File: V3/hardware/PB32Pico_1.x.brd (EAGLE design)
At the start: 33.3 x 10.8 mm, 27 parts, among them IC1 ESP32-PICO-D4UM-ESP32-PICO-D4, U1 AP2112K-3.3TRG1

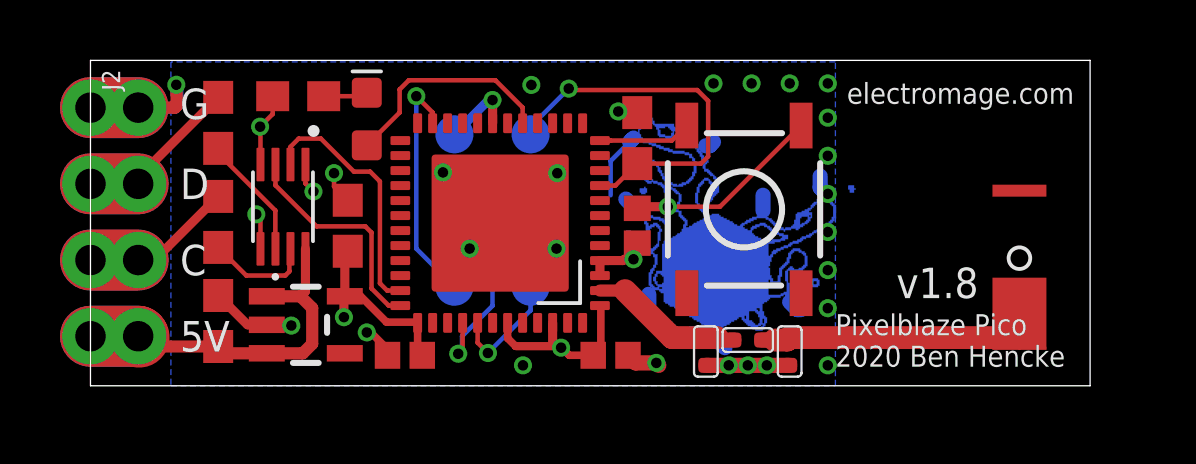
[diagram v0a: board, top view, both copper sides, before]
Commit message: PICO pcb reworked
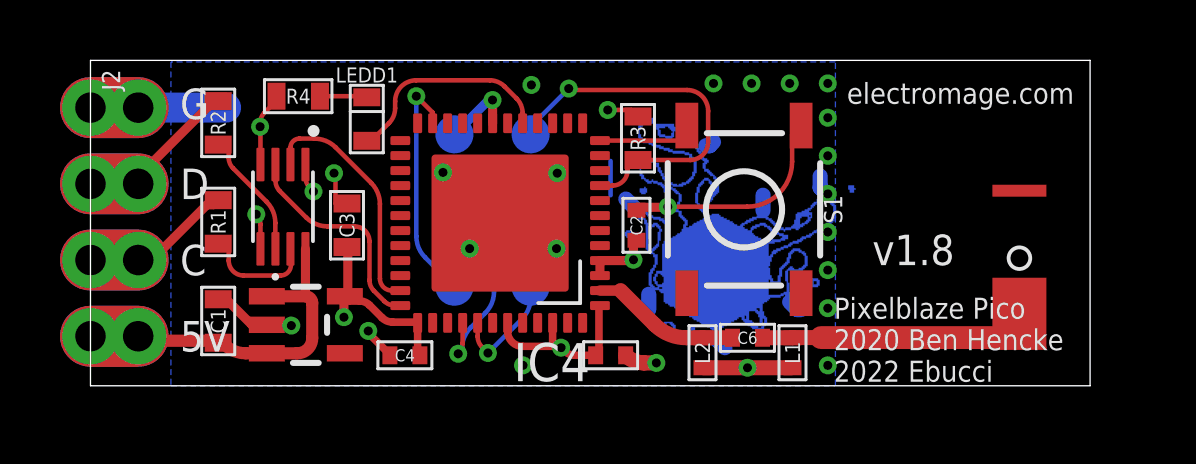
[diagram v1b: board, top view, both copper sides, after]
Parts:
- removed D1: (no value), SparkFun-LED:LED-0603
- removed IC1: ESP32-PICO-D4UM-ESP32-PICO-D4, bens:PICO-D4-QFN48
- removed U$1: SN74LVC2T45DCUR, SOP50P310X90-8N:SOP50P310X90-8N
- removed U1: AP2112K-3.3TRG1, SparkFun-PowerIC:SOT23-5
- added IC2: SN74LVC2T45DCUR, pixelblaze:SOP50P310X90-8N
- added IC3: 3.3V, pixelblaze:SOT23-5
- added IC4: ESP32-PICO-D4UM-ESP32-PICO-D4, pixelblaze:PICO-D4-QFN48
- added LEDD1: LED-0603, rc:LED0603
- C1, C3: device SparkFun-Capacitors:0603 -> rc:C0603
- C2, C4, C5: device SparkFun-Capacitors:0402 -> rc:C0402
- C6: device Seeed-Capacitor:C0402 -> rc:C0402
- L1, L2: value 1.8NH -> L-0402; device Seeed-Inductor:L0402 -> rc:L0402
- R1, R2, R3, R4: device SparkFun-Resistors:0603 -> rc:R0603
- S1: device SparkFun-Switches:TACTILE_SWITCH_SMD_5.2MM -> pixelblaze:TACTILE_SWITCH_SMD_5.2MM
- U$2: device bens:CHIPANTENNA-1206-SHORT -> pixelblaze:CHIPANTENNA-1206-SHORT
- moved L2 2.91 mm to (20.4, 1.10), turned to 270 degrees
- moved L1 2.89 mm to (23.4, 1.10), turned to 270 degrees
- moved C6 0.08 mm to (21.9, 1.60), turned to 180 degrees
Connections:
- net +3V3: now also IC2.1, IC2.5, IC3.5, IC4.1, IC4.19, IC4.3, IC4.37, IC4.4, IC4.43, IC4.46; no longer IC1.1, IC1.19, IC1.3, IC1.37, IC1.4, IC1.43, IC1.46, U$1.1, U$1.5, U1.5
- net +5V: now also IC2.8, IC3.1, IC3.3; no longer U$1.8, U1.1, U1.3
- net BUTTON: now also IC4.12; no longer IC1.12
- net EN: now also IC4.9; no longer IC1.9
- net GND: now also IC2.4, IC3.2, IC4.EXP, L1.2, L2.2; no longer IC1.EXP, L1.1, L2.1, U$1.4, U1.2
- net IO0: now also IC4.23; no longer IC1.23
- net IO12: now also IC4.18; no longer IC1.18
- net IO21: now also IC4.42; no longer IC1.42
- net N$1: now also L1.1; no longer L2.2
- net N$2: now also IC4.17, LEDD1.A; no longer D1.A, IC1.17
- net N$3: now also LEDD1.C; no longer D1.C
- net N$4: now also IC2.7; no longer U$1.7
- net N$5: now also IC2.6; no longer U$1.6
- net N$6: now also IC4.2, L2.1; no longer IC1.2, L1.2
- net SCK: now also IC2.2, IC4.35; no longer IC1.35, U$1.2
- net SDO: now also IC2.3, IC4.36; no longer IC1.36, U$1.3
- net SENSOR_CAPN: now also IC4.7; no longer IC1.7
- net U0TX: now also IC4.41; no longer IC1.41
- net UORX: now also IC4.40; no longer IC1.40
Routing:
- net GND: track 40.4 -> 37.7 mm, vias 27 -> 24
- net +3V3: track 22.2 -> 20.7 mm
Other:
- board text added: "Pixelblaze Pico 2020 Ben Hencke 2022 Ebucci"
